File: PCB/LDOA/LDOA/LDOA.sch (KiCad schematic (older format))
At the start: 41 parts, among them Q1 BC547, Q10 BS250, Q2 BC547, Q3 BC557, Q4 BC547, Q5 BC557, Q6 BC547, Q7 2N7000, Q8 IRF9520, Q9 BS250

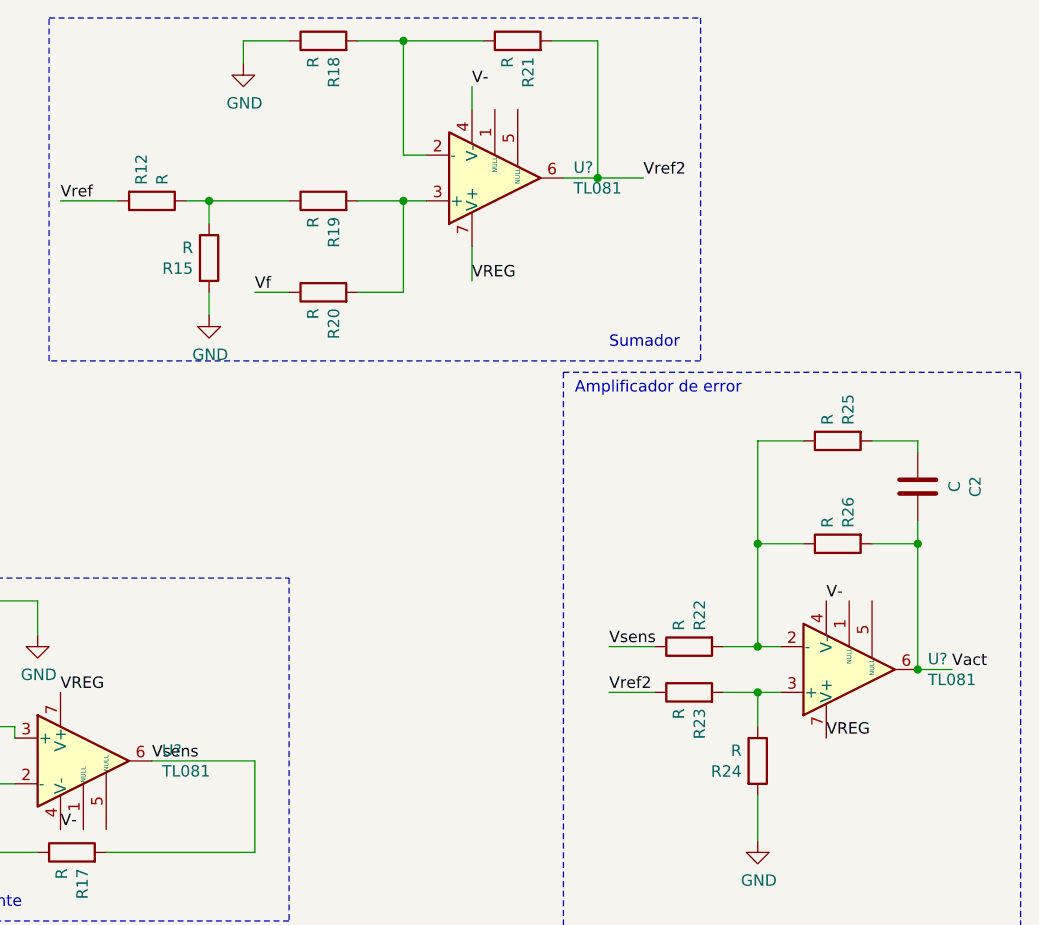
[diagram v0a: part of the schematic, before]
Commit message: Se agregaron mas pistas. Hay que avanzar con la inclusion del UVLO OVLO, terminales y demás
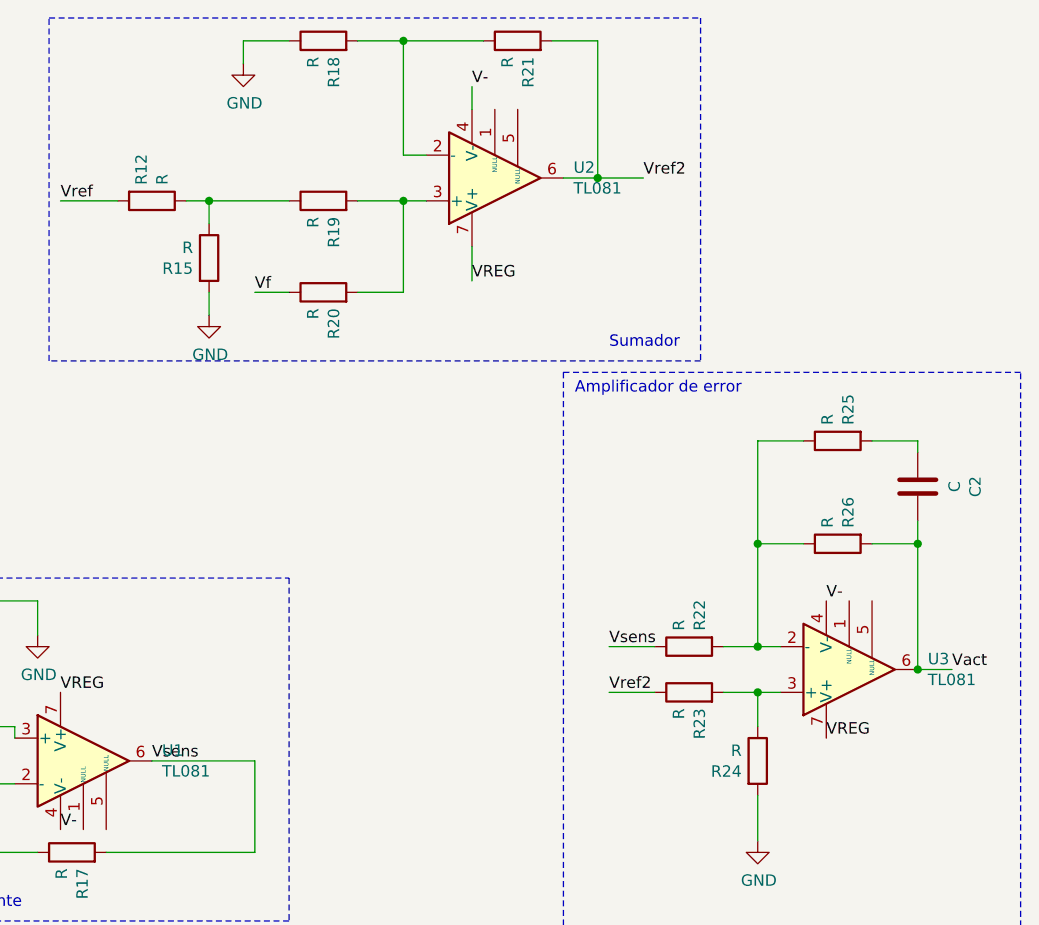
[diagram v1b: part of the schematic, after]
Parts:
- C1: footprint Capacitor_THT:CP_Radial_D17.0mm_P7.50mm -> Capacitor_THT:C_Disc_D5.0mm_W2.5mm_P5.00mm
- C2: footprint Capacitor_THT:CP_Radial_D17.0mm_P7.50mm -> Capacitor_THT:C_Disc_D4.7mm_W2.5mm_P5.00mm
- U1, U2, U3: renamed from U?; footprint (none) -> Package_DIP:DIP-8_W7.62mm
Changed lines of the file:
@@
 F 0 "C1" V 4098 3600 50  0000 C CNN
 F 1 "C" V 4189 3600 50  0000 C CNN
-F 2 "Capacitor_THT:CP_Radial_D17.0mm_P7.50mm" H 4388 3450 50  0001 C CNN
+F 2 "Capacitor_THT:C_Disc_D5.0mm_W2.5mm_P5.00mm" H 4388 3450 50  0001 C CNN
 F 3 "~" H 4350 3600 50  0001 C CNN
 	1    4350 3600
@@
 F 0 "C2" V 9398 2550 50  0000 C CNN
 F 1 "C" V 9489 2550 50  0000 C CNN
-F 2 "Capacitor_THT:CP_Radial_D17.0mm_P7.50mm" H 9688 2400 50  0001 C CNN
+F 2 "Capacitor_THT:C_Disc_D4.7mm_W2.5mm_P5.00mm" H 9688 2400 50  0001 C CNN
 F 3 "~" H 9650 2550 50  0001 C CNN
 	1    9650 2550
@@
 Wire Wire Line
 	1300 3700 1350 3700
-$Comp
-L Amplifier_Operational:TL081 U?
-U 1 1 62A878D4
-P 6000 3750
-F 0 "U?" H 6344 3796 50  0000 L CNN
-F 1 "TL081" H 6344 3705 50  0000 L CNN
-F 2 "" H 6050 3800 50  0001 C CNN
-F 3 "http://www.ti.com/lit/ds/symlink/tl081.pdf" H 6150 3900 50  0001 C CNN
-	1    6000 3750
-	1    0    0    -1
-$EndComp
 Text Label 5900 3450 0    50   ~ 0
 VREG
@@
 V-
 $Comp
-L Amplifier_Operational:TL081 U?
+L Amplifier_Operational:TL081 U3
 U 1 1 62A8B621
 P 9350 3350
-F 0 "U?" H 9694 3304 50  0000 L CNN
+F 0 "U3" H 9694 3304 50  0000 L CNN
 F 1 "TL081" H 9694 3395 50  0000 L CNN
-F 2 "" H 9400 3400 50  0001 C CNN
+F 2 "Package_DIP:DIP-8_W7.62mm" H 9400 3400 50  0001 C CNN
 F 3 "http://www.ti.com/lit/ds/symlink/tl081.pdf" H 9500 3500 50  0001 C CNN
 	1    9350 3350
@@
 V-
 $Comp
-L Amplifier_Operational:TL081 U?
+L Amplifier_Operational:TL081 U2
 U 1 1 62A94557
 P 7800 1200
-F 0 "U?" H 8144 1154 50  0000 L CNN
+F 0 "U2" H 8144 1154 50  0000 L CNN
 F 1 "TL081" H 8144 1245 50  0000 L CNN
-F 2 "" H 7850 1250 50  0001 C CNN
+F 2 "Package_DIP:DIP-8_W7.62mm" H 7850 1250 50  0001 C CNN
 F 3 "http://www.ti.com/lit/ds/symlink/tl081.pdf" H 7950 1350 50  0001 C CNN
 	1    7800 1200
@@
 Text Notes 2700 5700 0    50   ~ 0
 Realimentador\n
+$Comp
+L Amplifier_Operational:TL081 U1
+U 1 1 62A878D4
+P 6000 3750
+F 0 "U1" H 6344 3796 50  0000 L CNN
+F 1 "TL081" H 6344 3705 50  0000 L CNN
+F 2 "Package_DIP:DIP-8_W7.62mm" H 6050 3800 50  0001 C CNN
+F 3 "http://www.ti.com/lit/ds/symlink/tl081.pdf" H 6150 3900 50  0001 C CNN
+	1    6000 3750
+	1    0    0    -1
+$EndComp
 $EndSCHEMATC
